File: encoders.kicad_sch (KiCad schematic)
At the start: 2 parts, among them J7 Conn_01x04, J8 Conn_01x04

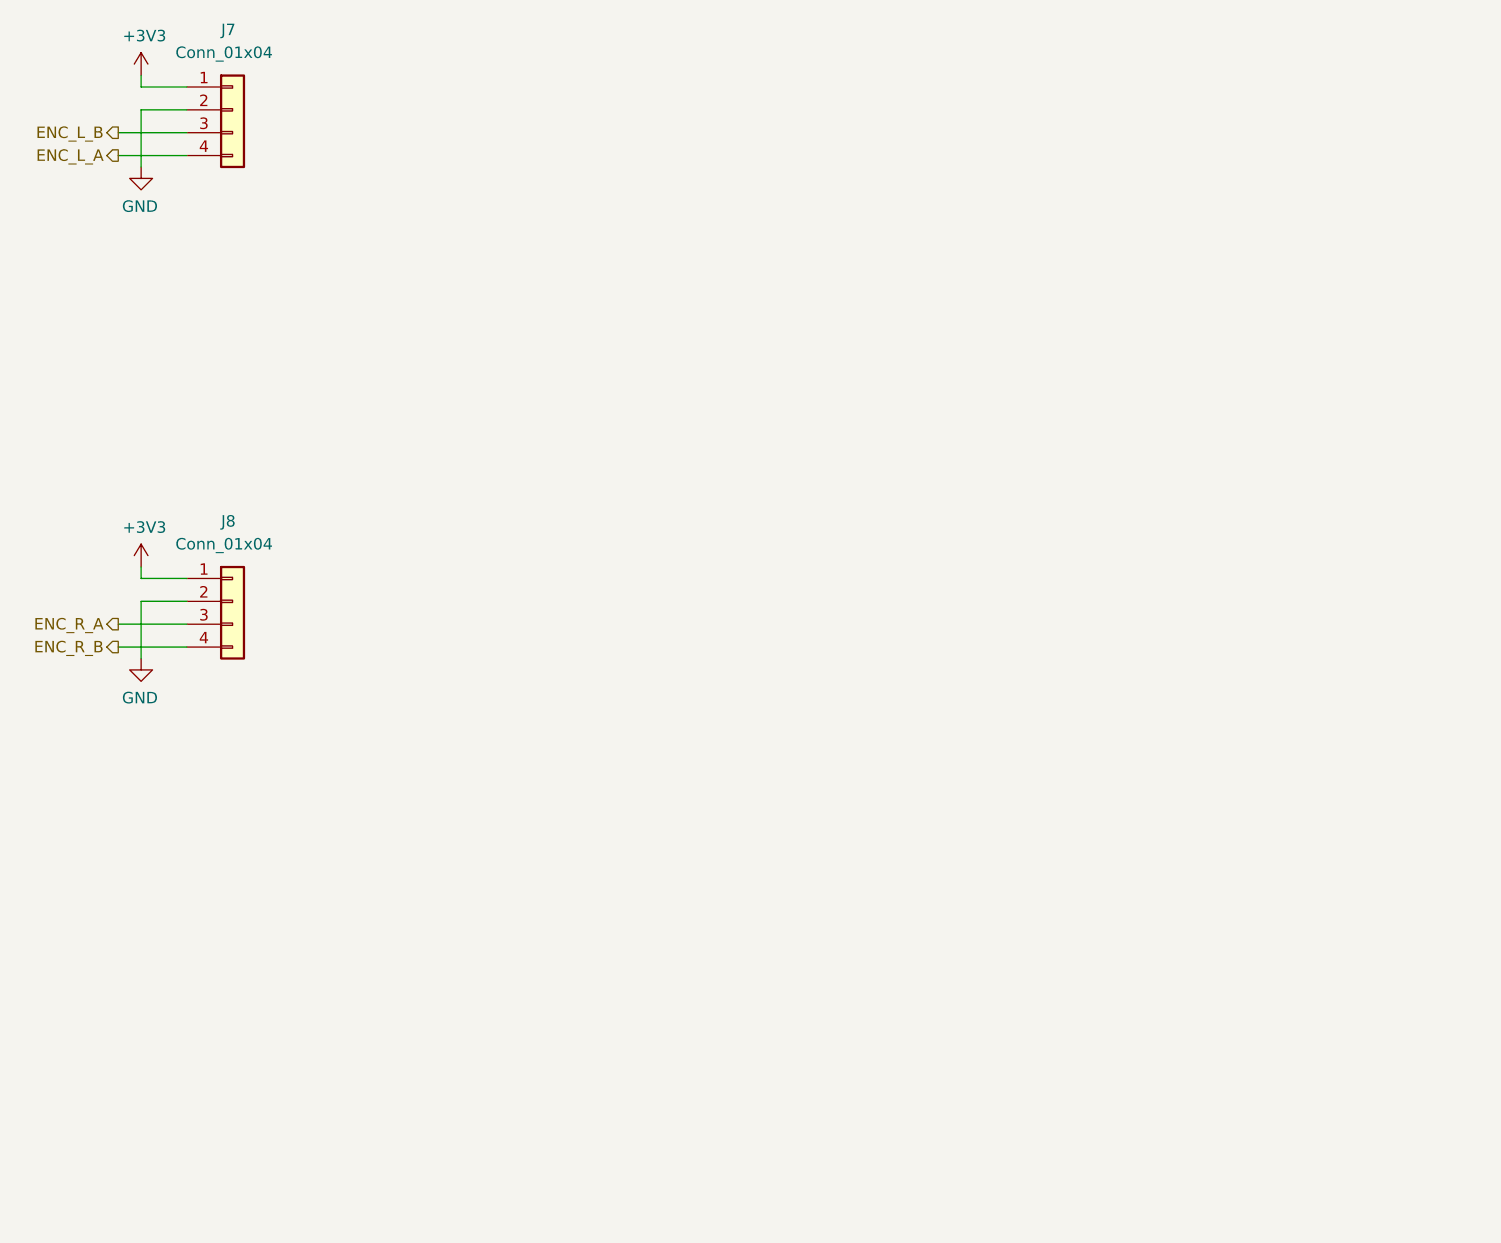
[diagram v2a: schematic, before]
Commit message: Cleanup encoders schematic
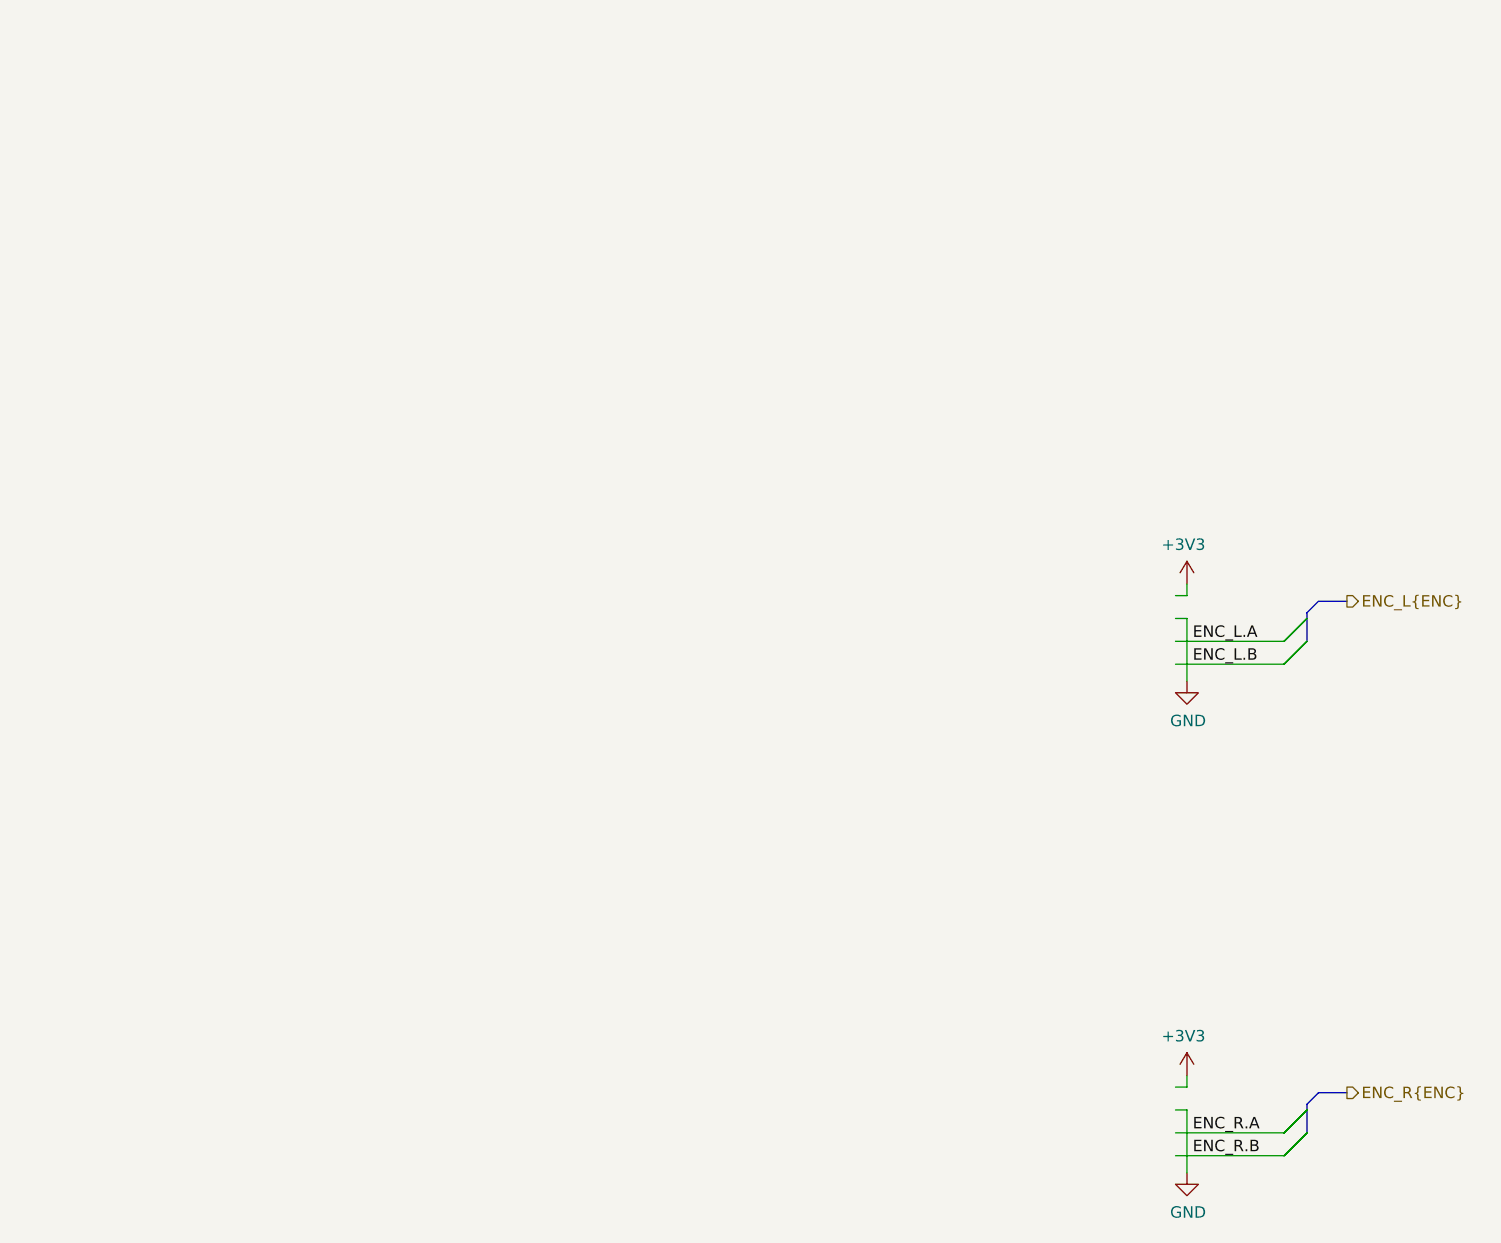
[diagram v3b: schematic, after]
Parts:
- removed J7, J8: Conn_01x04, connector_brd2brd:01x04_1.0x0.5mm_SMD, symbol Connector_Generic:Conn_01x04

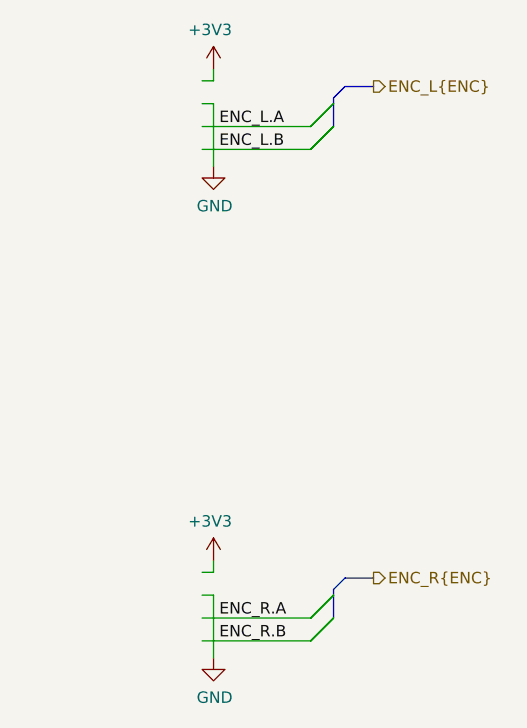
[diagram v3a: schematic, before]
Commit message: Add footprint for AS3504 boards
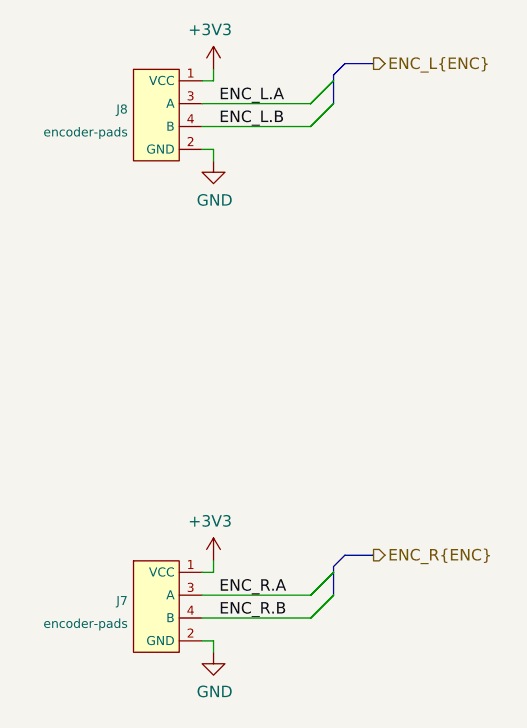
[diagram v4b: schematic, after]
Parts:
- added J7, J8: encoder-pads, synermycha-electronics:01x04_1.0x0.5mm_SMD, symbol synermycha-electronics:encoder-pads
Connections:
- net +3V3: now also J7.1 (VCC), J8.1 (VCC)
- net ENC_L.A: now also J8.3 (A)
- net ENC_L.B: now also J8.4 (B)
- net ENC_R.A: now also J7.3 (A)
- net ENC_R.B: now also J7.4 (B)
- net GND: now also J7.2 (GND), J8.2 (GND)

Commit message: Loclib, cleanup
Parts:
- J7, J8: footprint synermycha-electronics:01x04_1.0x0.5mm_SMD -> synermycha-electronics-footprints:01x04_1.0x0.5mm_SMD
